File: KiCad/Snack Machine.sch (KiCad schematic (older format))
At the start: 160 parts, among them J1 MDB, J10 Row Screw Terminal, J11 Column Screw Terminal, J12 Display Serial Header, J13 RFID_CONNECTOR, J14 Large Display Header, J2 Power Screw Terminal, J3 RFID Serial Connector, J4 RFID Led Connector, J5 MDB, J6 Conn_01x02, J7 LCD EXP1, J8 LCD EXP2, J9 AVR-ISP-6, Q1 P-CH 30V 3.8A, Q26 MMBT3904, Q27 BSS138, Q28 BSS138, SW1 SW_SPST, U2 MEZD71202A-G, U3 ATmega2560-16AU, U7 Huzzah32, Y1 16MHz

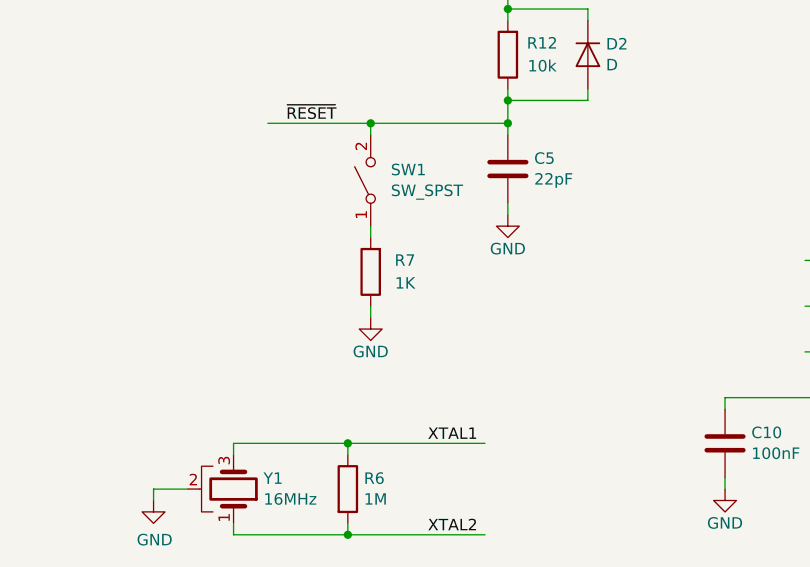
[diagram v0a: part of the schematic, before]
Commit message: Updating a ton of part numbers
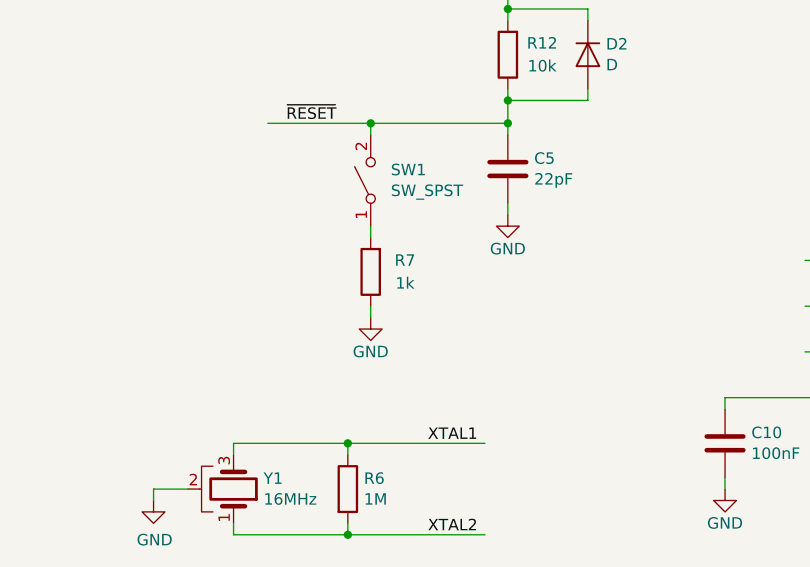
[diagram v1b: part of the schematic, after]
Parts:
- C10, C11, C12, C13, C14, C15: Manufacturer (none) -> Yageo; Part Number (none) -> CC0603KRX7R9BB104
- C16: Manufacturer (none) -> TDK; Part Number (none) -> C1608X7R1A105K080AC
- C5: Manufacturer (none) -> KEMET; Part Number (none) -> C0603C220J1GACTU
- J13: Manufacturer (none) -> Molex; Part Number (none) -> 70543-0004
- Q26: Manufacturer (none) -> MCC; Part Number (none) -> MMBT3904-TP
- Q27: Manufacturer (none) -> ON Semiconductor; Part Number (none) -> BSS138
- R1, R10, R11, R13, R14, R15, R16, R2, R8, R9: Manufacturer (none) -> Yageo; Part Number (none) -> RC0603JR-070RL
- R12, R3, R4, R90, R91, R92, R93: Manufacturer (none) -> Yageo; Part Number (none) -> RC0603FR-0710KL
- R17, R18, R5: Manufacturer (none) -> Yageo; Part Number (none) -> RC0603FR-071KL
- R6: Manufacturer (none) -> Yageo; Part Number (none) -> RC0603FR-071ML
- R7: value 1K -> 1k; Manufacturer (none) -> Yageo; Part Number (none) -> RC0603FR-071KL
- R88, R89: Manufacturer (none) -> Yageo; Part Number (none) -> RC0603FR-074K7L

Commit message: fixed a few small issues
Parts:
- added TP94: TestPoint, Snack Machine:TestPoint_THTPad_D0.8mm_Drill0.4mm, symbol Connector:TestPoint
- Q27, Q28: footprint Package_TO_SOT_SMD:SOT-23 -> Snack Machine:SOT-23_Handsoldering_Lite
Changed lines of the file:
@@
 F 0 "Q28" V 5750 5950 50  0000 C CNN
 F 1 "BSS138" V 5841 6000 50  0000 C CNN
-F 2 "Package_TO_SOT_SMD:SOT-23" H 5700 5925 50  0001 L CIN
+F 2 "Snack Machine:SOT-23_Handsoldering_Lite" H 5700 5925 50  0001 L CIN
 F 3 "https://www.fairchildsemi.com/datasheets/BS/BSS138.pdf" H 5500 6000 50  0001 L CNN
 	1    5500 6000
@@
 F 0 "Q27" V 5750 4900 50  0000 C CNN
 F 1 "BSS138" V 5841 4950 50  0000 C CNN
-F 2 "Package_TO_SOT_SMD:SOT-23" H 5700 4875 50  0001 L CIN
+F 2 "Snack Machine:SOT-23_Handsoldering_Lite" H 5700 4875 50  0001 L CIN
 F 3 "https://www.fairchildsemi.com/datasheets/BS/BSS138.pdf" H 5500 4950 50  0001 L CNN
 F 4 "BSS138" V 5500 4950 50  0001 C CNN "Part Number"
@@
 Wire Wire Line
 	14700 1250 14900 1250
+$Comp
+L Connector:TestPoint TP?
+U 1 1 5C5AD102
+P 9900 3900
+AR Path="/5BCD883C/5C5AD102" Ref="TP?"  Part="1"
+AR Path="/5C5AD102" Ref="TP94"  Part="1"
+F 0 "TP94" V 9850 3850 50  0000 L CNN
+F 1 "TestPoint" V 9850 4100 50  0000 L CNN
+F 2 "Snack Machine:TestPoint_THTPad_D0.8mm_Drill0.4mm" H 10100 3900 50  0001 C CNN
+F 3 "~" H 10100 3900 50  0001 C CNN
+	1    9900 3900
+	0    1    1    0
+$EndComp
 $EndSCHEMATC

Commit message: Making a bunch of changes throughout the board
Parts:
- removed J1: MDB, Connector_Molex:Molex_Mini-Fit_Jr_5566-06A_2x03_P4.20mm_Vertical, symbol Connector_Generic:Conn_02x03_Top_Bottom
- removed Q27, Q28: BSS138, Snack Machine:SOT-23_Handsoldering_Lite, symbol Transistor_FET:BSS138
- removed R17, R18: 1k, Resistor_SMD:R_0603_1608Metric_Pad1.05x0.95mm_HandSolder, symbol Device:R
- removed R2: 0R, Resistor_SMD:R_0603_1608Metric_Pad1.05x0.95mm_HandSolder, symbol Device:R
- removed R90, R91, R92, R93: 10k, Resistor_SMD:R_0603_1608Metric_Pad1.05x0.95mm_HandSolder, symbol Device:R
- removed TP10, TP11, TP12, TP13, TP14, TP2, TP28, TP3, TP4, TP5, TP6, TP7, TP8, TP9, TP94: TestPoint, Snack Machine:TestPoint_THTPad_D0.8mm_Drill0.4mm, symbol Connector:TestPoint
- removed U7: Huzzah32, Snack Machine:HUZZAH32, symbol Snack_Machine:Huzzah32
- R1: value 0R -> 1k; Part Number RC0603JR-070RL -> RC0603FR-0710KL
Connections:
- net labels added: LCD_4, LCD_5, LCD_6, LCD_7, LCD_BEEP, LCD_EN, LCD_RESET, MOTOR_FAULT, SD_CS, SD_DET
- net labels removed: +3.3V, BEEPER, CS, HUZZAH_RX, HUZZAH_TX, LCD_PB, LCD_SCL, LCD_SDA, SCL, SDA
- wire segments 419 -> 360
- no-connect marks 30 -> 5
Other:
- note added: "LCD_RESET?"
- note added: "Slave CS"
- note added: "TODO: Consider removing"

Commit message: Combining RFID to 1 header and improving 4D LCD stuff
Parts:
- removed J12: Display Serial Header, Connector_PinSocket_2.54mm:PinSocket_2x05_P2.54mm_Vertical, symbol Connector_Generic:Conn_02x05_Odd_Even
- removed J13: RFID_CONNECTOR, Connector_PinHeader_2.54mm:PinHeader_1x05_P2.54mm_Vertical, symbol Connector:Conn_01x05_Male
- removed J14: Large Display Header, Connector_PinSocket_2.54mm:PinSocket_2x15_P2.54mm_Vertical, symbol Connector_Generic:Conn_02x15_Counter_Clockwise
- removed J3: RFID Serial Connector, Connector_PinHeader_2.54mm:PinHeader_1x05_P2.54mm_Vertical, symbol Connector:Conn_01x05_Female
- removed J4: RFID Led Connector, Connector_PinHeader_2.54mm:PinHeader_1x03_P2.54mm_Vertical, symbol Connector:Conn_01x03_Female
- removed Q26: MMBT3904, Snack Machine:SOT-23_Handsoldering_Lite, symbol Transistor_BJT:MMBT3904
- removed R8, R9: 0R, Resistor_SMD:R_0603_1608Metric_Pad1.05x0.95mm_HandSolder, symbol Device:R
- removed R88, R89: 4.7k, Resistor_SMD:R_0603_1608Metric_Pad1.05x0.95mm_HandSolder, symbol Device:R
- removed TP1, TP50, TP51, TP52, TP53, TP54, TP55, TP56, TP57, TP58, TP59, TP60, TP61, TP62, TP63, TP64, TP65, TP66, TP67, TP68, TP69, TP70, TP71, TP72, TP73, TP74, TP75, TP76, TP77, TP78, TP79, TP80, TP81, TP82, TP83, TP84: TestPoint, Snack Machine:TestPoint_THTPad_D0.8mm_Drill0.4mm, symbol Connector:TestPoint
- added J?: RFID_CONNECTOR, symbol Connector:Conn_01x10_Male
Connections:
- net labels added: BEEP_CTRL, RFID_5V, RFID_CARD_PRESENT, RFID_GND, RFID_GRN_LED, RFID_HOLD, RFID_SHIELD_GND
- net labels removed: RFID_BEEP, RFID_LED, RFID_RX, RFID_TX, RX_DISPLAY, TX_DISPLAY
- wire segments 360 -> 294
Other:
- note removed: "TODO: Consider removing"

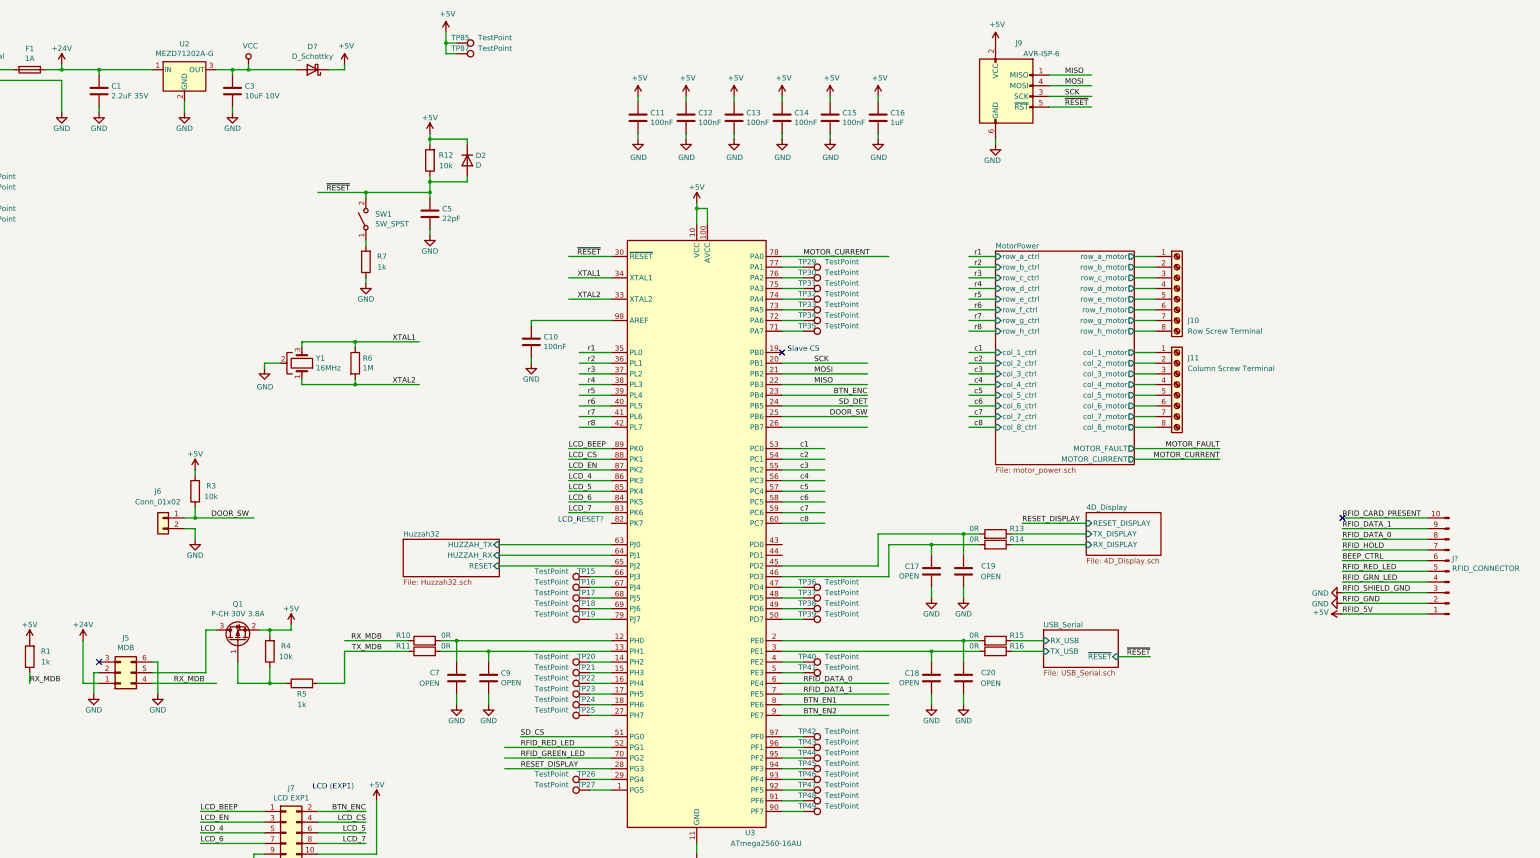
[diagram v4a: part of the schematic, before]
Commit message: Fixing ERC rules
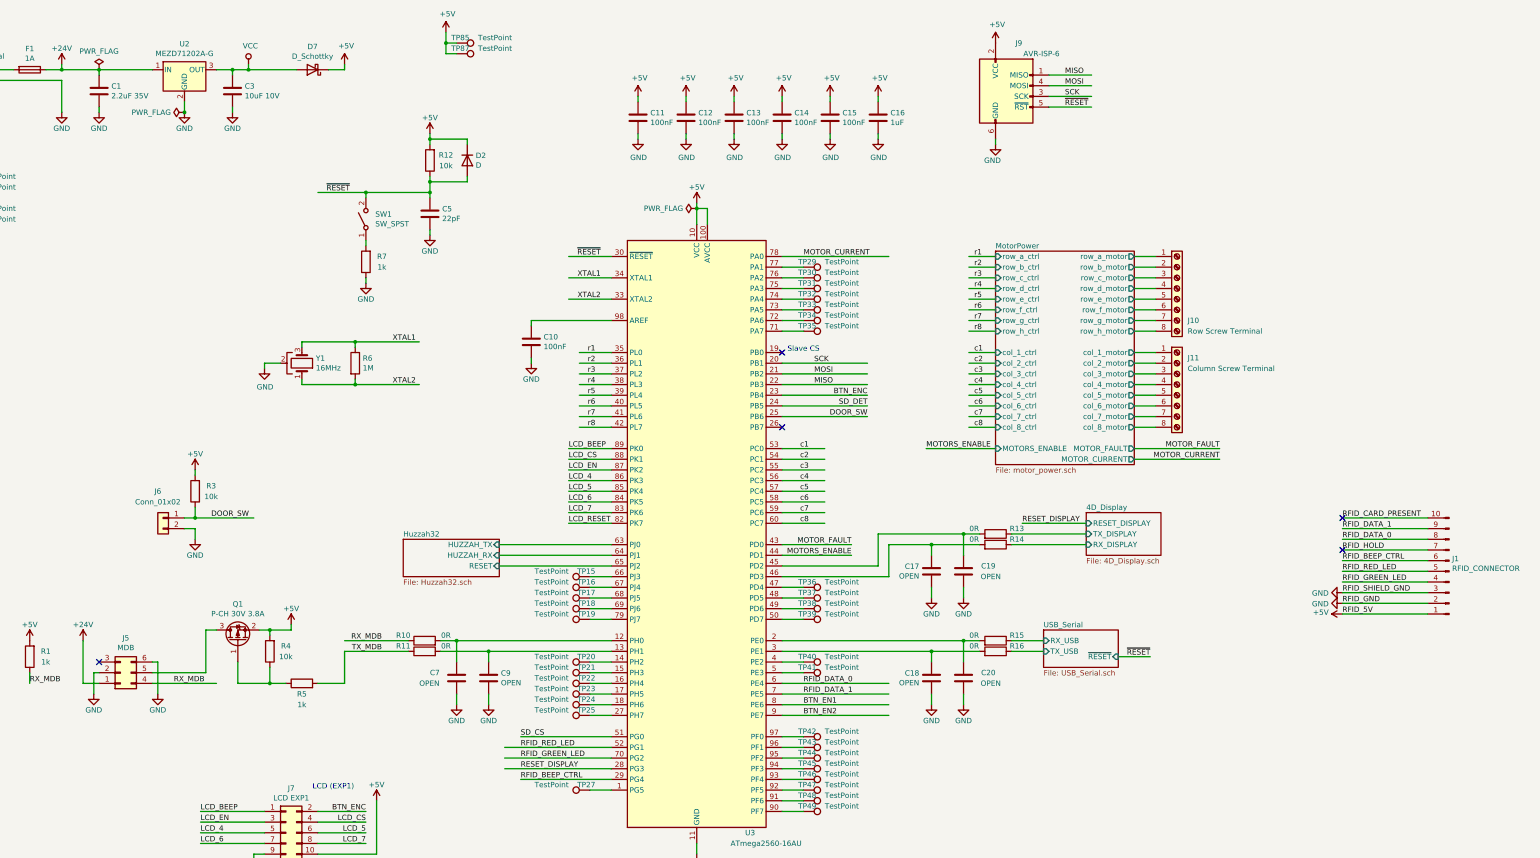
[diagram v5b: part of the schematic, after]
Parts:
- removed TP26: TestPoint, Snack Machine:TestPoint_THTPad_D0.8mm_Drill0.4mm, symbol Connector:TestPoint
- gave numbers to parts that had none: 1
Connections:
- net labels added: MOTORS_ENABLE, RFID_BEEP_CTRL
- net labels removed: BEEP_CTRL, RFID_GRN_LED
- wire segments 294 -> 297
- no-connect marks 5 -> 7
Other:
- note removed: "LCD_RESET?"
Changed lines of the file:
@@
 F34 "MOTOR_CURRENT" O R 12400 4900 50
 F35 "MOTOR_FAULT" O R 12400 4800 50
+F36 "MOTORS_ENABLE" I L 11100 4800 50
 $EndSheet
 $Comp
@@
 Wire Wire Line
 	6500 7700 7500 7700
-Wire Wire Line
-	9100 4600 9900 4600
 $Comp
 L Connector_Generic:Conn_02x03_Top_Bottom J5
@@
 $Comp
 L Connector:TestPoint TP?
-U 1 1 5C7B37A7
-P 7300 7900
-AR Path="/5BCD883C/5C7B37A7" Ref="TP?"  Part="1"
-AR Path="/5C7B37A7" Ref="TP26"  Part="1"
-F 0 "TP26" V 7250 7850 50  0000 L CNN
-F 1 "TestPoint" V 7250 8100 50  0000 L CNN
-F 2 "Snack Machine:TestPoint_THTPad_D0.8mm_Drill0.4mm" H 7500 7900 50  0001 C CNN
-F 3 "~" H 7500 7900 50  0001 C CNN
-	1    7300 7900
-	0    -1   1    0
-$EndComp
-Wire Wire Line
-	7300 7900 7500 7900
-$Comp
-L Connector:TestPoint TP?
 U 1 1 5C7D0641
 P 7300 7300
@@
 Wire Wire Line
 	6650 7500 7500 7500
-Text Notes 7000 5500 0    50   ~ 0
-LCD_RESET?
 Wire Wire Line
 	9100 3000 10100 3000
@@
 	10100 5700 10500 5700
 $Comp
-L Connector:Conn_01x10_Male J?
+L Connector:Conn_01x10_Male J1
 U 1 1 5DB7B643
 P 15350 5950
-F 0 "J?" H 15322 5832 50  0000 R CNN
+F 0 "J1" H 15322 5832 50  0000 R CNN
 F 1 "RFID_CONNECTOR" H 15322 5923 50  0000 R CNN
 F 2 "" H 15350 5950 50  0001 C CNN
@@
 RFID_SHIELD_GND
 Text Label 14350 6050 0    50   ~ 0
-RFID_GRN_LED
+RFID_GREEN_LED
 Text Label 14350 5950 0    50   ~ 0
 RFID_RED_LED
 Text Label 14350 5850 0    50   ~ 0
-BEEP_CTRL
+RFID_BEEP_CTRL
 Text Label 14350 5750 0    50   ~ 0
 RFID_HOLD
@@
 NoConn ~ 14350 5450
 $Comp
-L power:+5V #PWR?
+L power:+5V #PWR0108
 U 1 1 5DD0CE86
 P 14350 6350
-F 0 "#PWR?" H 14350 6200 50  0001 C CNN
+F 0 "#PWR0108" H 14350 6200 50  0001 C CNN
 F 1 "+5V" V 14365 6478 50  0000 L CNN
 F 2 "" H 14350 6350 50  0001 C CNN
@@
 $EndComp
 $Comp
-L power:GND #PWR?
+L power:GND #PWR0109
 U 1 1 5DD3BEF7
 P 14350 6250
-F 0 "#PWR?" H 14350 6000 50  0001 C CNN
+F 0 "#PWR0109" H 14350 6000 50  0001 C CNN
 F 1 "GND" V 14355 6122 50  0000 R CNN
 F 2 "" H 14350 6250 50  0001 C CNN
@@
 $EndComp
 $Comp
-L power:GND #PWR?
+L power:GND #PWR0110
 U 1 1 5DD3C2B3
 P 14350 6150
-F 0 "#PWR?" H 14350 5900 50  0001 C CNN
+F 0 "#PWR0110" H 14350 5900 50  0001 C CNN
 F 1 "GND" V 14355 6022 50  0000 R CNN
 F 2 "" H 14350 6150 50  0001 C CNN
@@
 Wire Wire Line
 	12550 6750 12250 6750
+$Comp
+L power:PWR_FLAG #FLG0101
+U 1 1 5DB55FD9
+P 2700 1250
+F 0 "#FLG0101" H 2700 1325 50  0001 C CNN
+F 1 "PWR_FLAG" H 2700 1423 50  0000 C CNN
+F 2 "" H 2700 1250 50  0001 C CNN
+F 3 "~" H 2700 1250 50  0001 C CNN
+	1    2700 1250
+	1    0    0    -1
+$EndComp
+$Comp
+L power:PWR_FLAG #FLG0102
+U 1 1 5DB5B741
+P 8300 2550
+F 0 "#FLG0102" H 8300 2625 50  0001 C CNN
+F 1 "PWR_FLAG" V 8300 2677 50  0000 L CNN
+F 2 "" H 8300 2550 50  0001 C CNN
+F 3 "~" H 8300 2550 50  0001 C CNN
+	1    8300 2550
+	0    -1   -1   0
+$EndComp
+$Comp
+L power:PWR_FLAG #FLG0103
+U 1 1 5DB5CE9B
+P 3500 1650
+F 0 "#FLG0103" H 3500 1725 50  0001 C CNN
+F 1 "PWR_FLAG" V 3500 1777 50  0000 L CNN
+F 2 "" H 3500 1650 50  0001 C CNN
+F 3 "~" H 3500 1650 50  0001 C CNN
+	1    3500 1650
+	0    -1   -1   0
+$EndComp
+Connection ~ 3500 1650
+Text Label 7100 5500 0    50   ~ 0
+LCD_RESET
+Wire Wire Line
+	7100 5500 7500 5500
+NoConn ~ 9100 4600
+Text Label 9750 5700 2    50   ~ 0
+MOTOR_FAULT
+NoConn ~ 14350 5750
+Text Label 6650 7900 0    50   ~ 0
+RFID_BEEP_CTRL
+Wire Wire Line
+	6650 7900 7500 7900
+Text Label 9750 5800 2    50   ~ 0
+MOTORS_ENABLE
+Wire Wire Line
+	9100 5700 9750 5700
+Wire Wire Line
+	9100 5800 9750 5800
+Text Label 10450 4800 0    50   ~ 0
+MOTORS_ENABLE
+Wire Wire Line
+	10450 4800 11100 4800
 $EndSCHEMATC

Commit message: Current WIP for board layout
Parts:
- removed C17, C18, C19, C20, C7, C9: OPEN, Capacitor_SMD:C_0603_1608Metric_Pad1.05x0.95mm_HandSolder, symbol Device:C
- removed D7: D_Schottky, Diode_SMD:D_SOD-323, symbol Device:D_Schottky
- removed H1, H2, H3, H4: MountingHole_Pad, MountingHole:MountingHole_3.5mm_Pad, symbol Mechanical:MountingHole_Pad
- removed R11: 0R, Resistor_SMD:R_0603_1608Metric_Pad1.05x0.95mm_HandSolder, symbol Device:R
- removed TP15, TP16, TP17, TP18, TP19, TP20, TP21, TP22, TP23, TP24, TP25, TP27, TP29, TP30, TP31, TP32, TP33, TP34, TP35, TP36, TP37, TP38, TP39, TP40, TP41, TP42, TP43, TP44, TP45, TP46, TP47, TP48, TP49, TP85, TP87, TP88, TP89, TP90, TP91: TestPoint, Snack Machine:TestPoint_THTPad_D0.8mm_Drill0.4mm, symbol Connector:TestPoint
- added TH1, TH2, TH3, TH4: tooling_hole, Snack Machine:tooling_hole_2.55, symbol Snack_Machine:tooling_hole
- J1: footprint (none) -> Connector_PinHeader_2.54mm:PinHeader_1x10_P2.54mm_Vertical; Part Number (none) -> 0705430009
- J6: footprint Connector_JST:JST_XH_B02B-XH-A_1x02_P2.50mm_Vertical -> Connector_PinHeader_2.54mm:PinHeader_1x02_P2.54mm_Vertical
- J7, J8: footprint Connector_PinHeader_2.54mm:PinHeader_2x05_P2.54mm_Vertical -> Snack Machine:PinHeader_2x05_P2.54mm_Vertical
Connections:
- net labels removed: VCC
- wire segments 297 -> 222
- no-connect marks 7 -> 40
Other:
- moved on the sheet: R5
